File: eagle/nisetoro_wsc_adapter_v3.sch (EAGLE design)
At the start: 29 parts, among them CN3 WSC LCD, Q1 MMBT2222A, Q2 MMBT2222A, U2 24LC00ST, U3 TLV1117-15

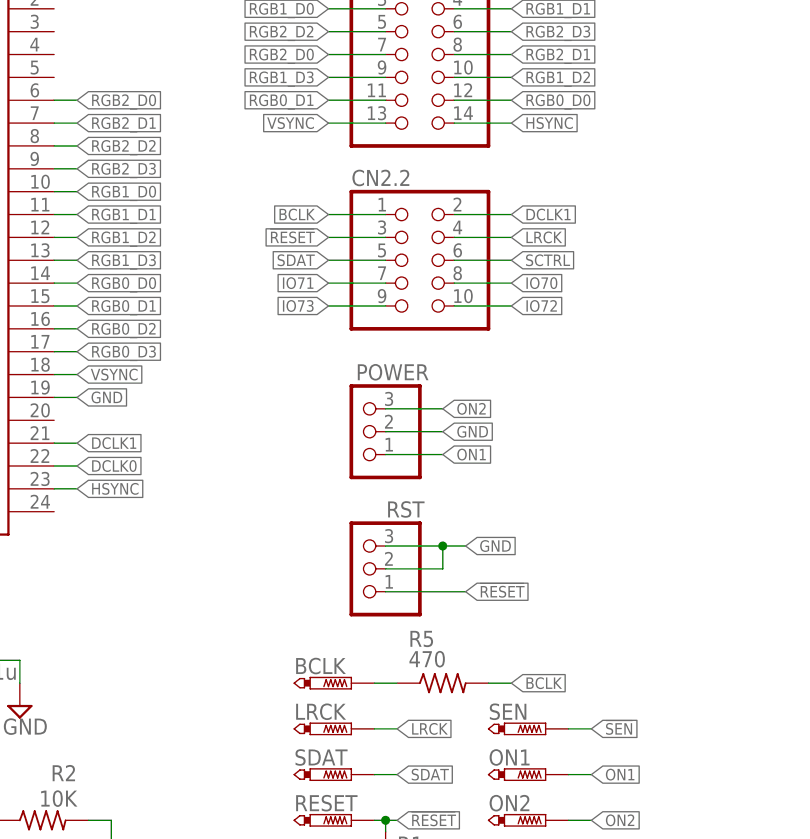
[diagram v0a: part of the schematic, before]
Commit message: EAGLE: Update adapter PCB to V3c
PREVIEW: Fix sound icon

MAX2: Set audio reg default value to 1 to match new version PCB
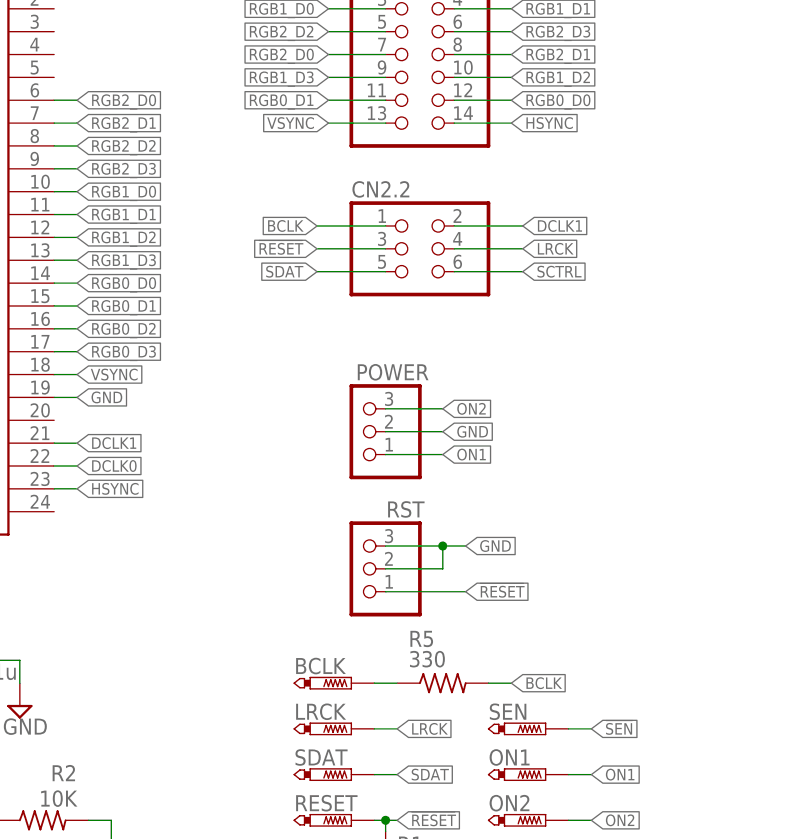
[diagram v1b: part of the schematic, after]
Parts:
- C1: device rcl:C-EUC0603 -> rcl:C-EUC0805
- CN2.2: device pinhead:PINHD-2X5 -> pinhead:PINHD-2X3
- R5: value 470 -> 330
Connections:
- removed net IO70: CN2.2.8
- removed net IO71: CN2.2.7
- removed net IO72: CN2.2.10
- removed net IO73: CN2.2.9
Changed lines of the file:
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@@
 <setting verticaltext="up"/>
 </settings>
-<grid distance="0.1" unitdist="inch" unit="inch" style="lines" multiple="1" display="no" altdistance="0.01" altunitdist="inch" altunit="inch"/>
+<grid distance="0.05" unitdist="inch" unit="inch" style="lines" multiple="1" display="yes" altdistance="0.01" altunitdist="inch" altunit="inch"/>
 <layers>
 <layer number="1" name="Top" color="4" fill="1" visible="no" active="no"/>
@@
 <part name="ON1" library="testpad" library_urn="urn:adsk.eagle:library:385" deviceset="PTR1" device="B1,27" package3d_urn="urn:adsk.eagle:package:27944/2"/>
 <part name="ON2" library="testpad" library_urn="urn:adsk.eagle:library:385" deviceset="PTR1" device="B1,27" package3d_urn="urn:adsk.eagle:package:27944/2"/>
-<part name="CN2.2" library="pinhead" library_urn="urn:adsk.eagle:library:325" deviceset="PINHD-2X5" device="" package3d_urn="urn:adsk.eagle:package:22470/2"/>
 <part name="V1" library="wirepad" library_urn="urn:adsk.eagle:library:412" deviceset="WIREPAD" device="SMD2,54-5,08" package3d_urn="urn:adsk.eagle:package:30841/1" value="BATT+"/>
 <part name="Q1" library="transistor-npn" library_urn="urn:adsk.eagle:library:398" deviceset="2N2222*" device="SOT23" package3d_urn="urn:adsk.eagle:package:28748/2" value="MMBT2222A"/>
@@
 <part name="+3V4" library="supply1" library_urn="urn:adsk.eagle:library:371" deviceset="+3V3" device=""/>
 <part name="SUPPLY3" library="supply2" library_urn="urn:adsk.eagle:library:372" deviceset="GND" device=""/>
-<part name="C1" library="rcl" library_urn="urn:adsk.eagle:library:334" deviceset="C-EU" device="C0603" package3d_urn="urn:adsk.eagle:package:23616/2" value="0.1u"/>
+<part name="C1" library="rcl" library_urn="urn:adsk.eagle:library:334" deviceset="C-EU" device="C0805" package3d_urn="urn:adsk.eagle:package:23617/2" value="0.1u"/>
 <part name="SUPPLY2" library="supply2" library_urn="urn:adsk.eagle:library:372" deviceset="GND" device=""/>
-<part name="R5" library="rcl" library_urn="urn:adsk.eagle:library:334" deviceset="R-US_" device="R0805" package3d_urn="urn:adsk.eagle:package:23553/2" value="470"/>
+<part name="R5" library="rcl" library_urn="urn:adsk.eagle:library:334" deviceset="R-US_" device="R0805" package3d_urn="urn:adsk.eagle:package:23553/2" value="330"/>
 <part name="Q2" library="transistor-npn" library_urn="urn:adsk.eagle:library:398" deviceset="2N2222*" device="SOT23" package3d_urn="urn:adsk.eagle:package:28748/2" value="MMBT2222A"/>
 <part name="SUPPLY4" library="supply2" library_urn="urn:adsk.eagle:library:372" deviceset="GND" device=""/>
 <part name="R4" library="rcl" library_urn="urn:adsk.eagle:library:334" deviceset="R-US_" device="R0805" package3d_urn="urn:adsk.eagle:package:23553/2" value="10K"/>
+<part name="CN2.2" library="pinhead" library_urn="urn:adsk.eagle:library:325" deviceset="PINHD-2X3" device="" package3d_urn="urn:adsk.eagle:package:22462/2"/>
 </parts>
 <sheets>
@@
 <attribute name="TP_SIGNAL_NAME" x="83.82" y="76.2" size="1.778" layer="97" rot="R270"/>
 </instance>
-<instance part="CN2.2" gate="A" x="71.12" y="139.7" smashed="yes">
-<attribute name="NAME" x="64.77" y="147.955" size="1.778" layer="95"/>
-<attribute name="VALUE" x="64.77" y="129.54" size="1.778" layer="96"/>
-</instance>
 <instance part="V1" gate="G$1" x="254" y="157.48" smashed="yes" rot="R180">
 <attribute name="NAME" x="252.857" y="159.3342" size="1.778" layer="95"/>
@@
 <attribute name="NAME" x="29.21" y="48.0314" size="1.778" layer="95" rot="R180"/>
 <attribute name="VALUE" x="29.21" y="42.672" size="1.778" layer="96" rot="R180"/>
+</instance>
+<instance part="CN2.2" gate="A" x="71.12" y="140.97" smashed="yes">
+<attribute name="NAME" x="64.77" y="146.685" size="1.778" layer="95"/>
+<attribute name="VALUE" x="64.77" y="133.35" size="1.778" layer="96"/>
 </instance>
 </instances>
@@
 <segment>
 <pinref part="CN2.2" gate="A" pin="3"/>
-<wire x1="68.58" y1="142.24" x2="62.23" y2="142.24" width="0.1524" layer="91"/>
-<label x="62.23" y="142.24" size="1.27" layer="95" rot="R180" xref="yes"/>
+<wire x1="68.58" y1="140.97" x2="60.96" y2="140.97" width="0.1524" layer="91"/>
+<label x="60.96" y="140.97" size="1.27" layer="95" rot="R180" xref="yes"/>
 </segment>
 </net>
@@
 <segment>
 <pinref part="CN2.2" gate="A" pin="5"/>
-<wire x1="68.58" y1="139.7" x2="62.23" y2="139.7" width="0.1524" layer="91"/>
-<label x="62.23" y="139.7" size="1.27" layer="95" rot="R180" xref="yes"/>
+<wire x1="68.58" y1="138.43" x2="60.96" y2="138.43" width="0.1524" layer="91"/>
+<label x="60.96" y="138.43" size="1.27" layer="95" rot="R180" xref="yes"/>
 </segment>
 </net>
@@
 <segment>
 <pinref part="CN2.2" gate="A" pin="4"/>
-<wire x1="76.2" y1="142.24" x2="82.55" y2="142.24" width="0.1524" layer="91"/>
-<label x="82.55" y="142.24" size="1.27" layer="95" xref="yes"/>
+<wire x1="76.2" y1="140.97" x2="83.82" y2="140.97" width="0.1524" layer="91"/>
+<label x="83.82" y="140.97" size="1.27" layer="95" xref="yes"/>
 </segment>
 </net>
@@
 <segment>
 <pinref part="CN2.2" gate="A" pin="2"/>
-<wire x1="76.2" y1="144.78" x2="82.55" y2="144.78" width="0.1524" layer="91"/>
-<label x="82.55" y="144.78" size="1.27" layer="95" xref="yes"/>
+<wire x1="76.2" y1="143.51" x2="83.82" y2="143.51" width="0.1524" layer="91"/>
+<label x="83.82" y="143.51" size="1.27" layer="95" xref="yes"/>
 </segment>
 </net>
@@
 <wire x1="76.2" y1="157.48" x2="82.55" y2="157.48" width="0.1524" layer="91"/>
 <label x="82.55" y="157.48" size="1.27" layer="95" xref="yes"/>
-</segment>
-</net>
-<net name="IO70" class="0">
-<segment>
-<pinref part="CN2.2" gate="A" pin="8"/>
-<wire x1="76.2" y1="137.16" x2="82.55" y2="137.16" width="0.1524" layer="91"/>
-<label x="82.55" y="137.16" size="1.27" layer="95" xref="yes"/>
-</segment>
-</net>
-<net name="IO71" class="0">
-<segment>
-<pinref part="CN2.2" gate="A" pin="7"/>
-<wire x1="68.58" y1="137.16" x2="62.23" y2="137.16" width="0.1524" layer="91"/>
-<label x="62.23" y="137.16" size="1.27" layer="95" rot="R180" xref="yes"/>
-</segment>
-</net>
-<net name="IO73" class="0">
-<segment>
-<pinref part="CN2.2" gate="A" pin="9"/>
-<wire x1="68.58" y1="134.62" x2="62.23" y2="134.62" width="0.1524" layer="91"/>
-<label x="62.23" y="134.62" size="1.27" layer="95" rot="R180" xref="yes"/>
-</segment>
-</net>
-<net name="IO72" class="0">
-<segment>
-<pinref part="CN2.2" gate="A" pin="10"/>
-<wire x1="76.2" y1="134.62" x2="82.55" y2="134.62" width="0.1524" layer="91"/>
-<label x="82.55" y="134.62" size="1.27" layer="95" xref="yes"/>
 </segment>
 </net>
@@
 <segment>
 <pinref part="CN2.2" gate="A" pin="1"/>
-<wire x1="68.58" y1="144.78" x2="62.23" y2="144.78" width="0.1524" layer="91"/>
-<label x="62.23" y="144.78" size="1.27" layer="95" rot="R180" xref="yes"/>
+<wire x1="68.58" y1="143.51" x2="60.96" y2="143.51" width="0.1524" layer="91"/>
+<label x="60.96" y="143.51" size="1.27" layer="95" rot="R180" xref="yes"/>
 </segment>
 </net>
 <net name="SCTRL" class="0">
-<segment>
-<pinref part="CN2.2" gate="A" pin="6"/>
-<wire x1="76.2" y1="139.7" x2="82.55" y2="139.7" width="0.1524" layer="91"/>
-<label x="82.55" y="139.7" size="1.27" layer="95" xref="yes"/>
-</segment>
 <segment>
 <pinref part="R4" gate="G$1" pin="1"/>
@@
 <label x="17.78" y="44.45" size="1.27" layer="95" rot="R180" xref="yes"/>
 </segment>
-</net>
+<segment>
+<pinref part="CN2.2" gate="A" pin="6"/>
+<wire x1="76.2" y1="138.43" x2="83.82" y2="138.43" width="0.1524" layer="91"/>
+<label x="83.82" y="138.43" size="1.27" layer="95" xref="yes"/>
+</segment>
+</net>
